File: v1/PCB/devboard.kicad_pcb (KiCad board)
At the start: 2 copper layers, 51 x 21 mm, 32 parts, among them J1 USB_C_Receptacle_USB2.0_14P, J2 Conn_01x20, J3 Conn_01x20, J4 Conn_01x03, SW1 SW_Push, U1 RP2040, U2 MCP1700x-330xxTT, U3 W25Q16JVUXIQ TR, Y1 Crystal_GND24

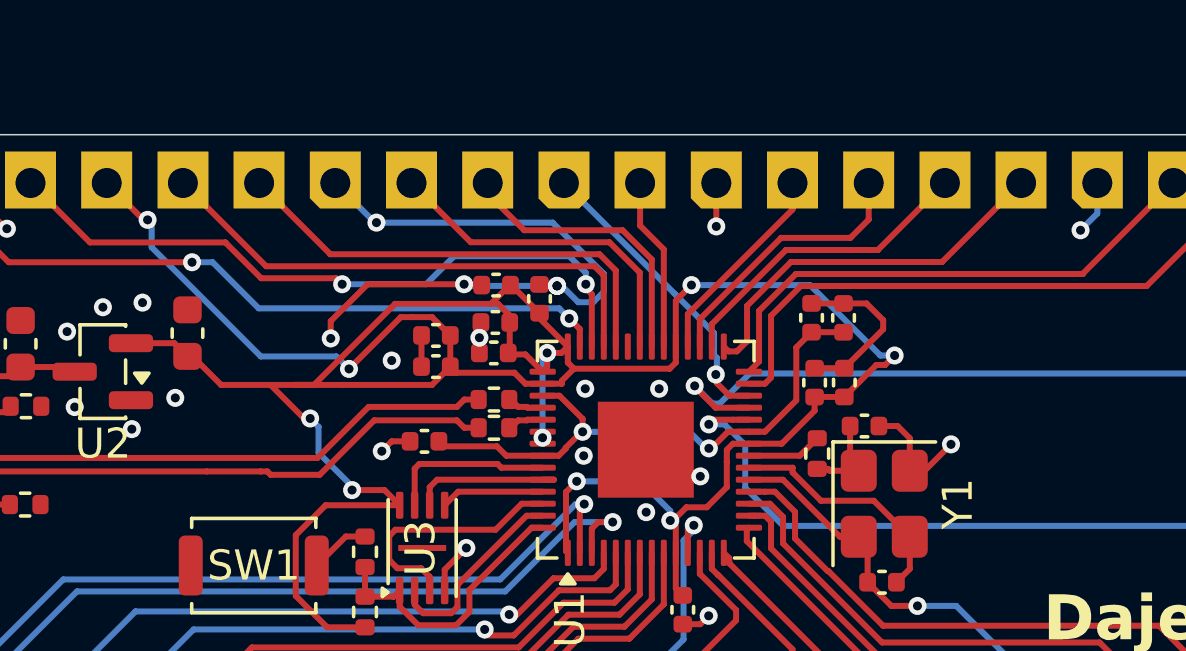
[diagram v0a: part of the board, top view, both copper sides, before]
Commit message: added v1 folder
added leds to the v1 board and created a v2 folder
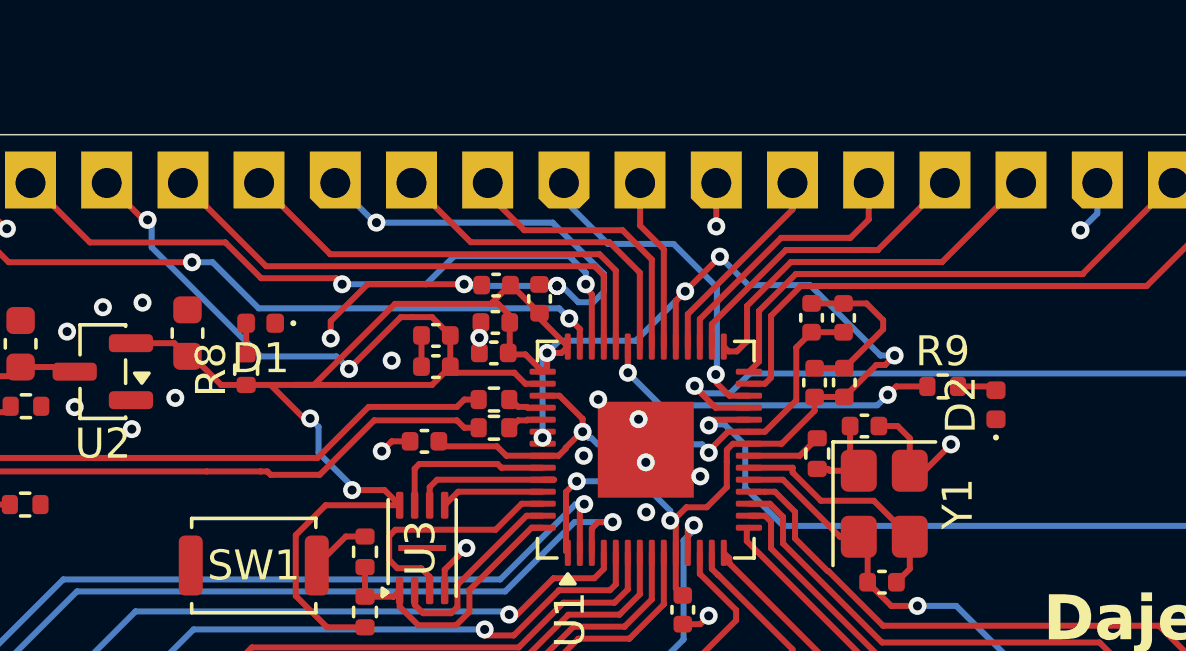
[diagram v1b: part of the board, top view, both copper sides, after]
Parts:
- added D1: LED, LED_SMD:LED_0402_1005Metric, F.Cu at (105.8, 63.3)
- added D2: LED, LED_SMD:LED_0402_1005Metric, F.Cu at (130.3, 66.0)
- added R8: 1K, Resistor_SMD:R_0402_1005Metric, F.Cu at (105.3, 64.8)
- added R9: 1K, Resistor_SMD:R_0402_1005Metric, F.Cu at (128.6, 65.4)
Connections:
- U1 pad 37: unconnected-(U1-GPIO25-Pad37) -> led2
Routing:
- net led2: track 0.00 -> 11.6 mm, vias 0 -> 2
- net RUN: track 10.1 -> 11.6 mm
- net Net-(D2-A): track 0.00 -> 1.32 mm
- net Net-(D1-A): track 0.00 -> 1.04 mm
- net +3.3V: track 103.2 -> 103.3 mm, vias 10 -> 11
- net GND: vias 34 -> 35
